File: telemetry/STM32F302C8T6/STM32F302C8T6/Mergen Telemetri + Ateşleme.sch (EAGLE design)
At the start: 91 parts, among them J2 U.FL, Q2 IRLML6344TRPBF, Q3 IRLML6344TRPBF, U2 BMP280, U3 MPU-6050, U4 L86, U6 AMS1117-3.3, U7 AMS1117-3.3, U8 STM32F302C8T6, Y2 ABM3B-26.000MHZ-10-1-U-T

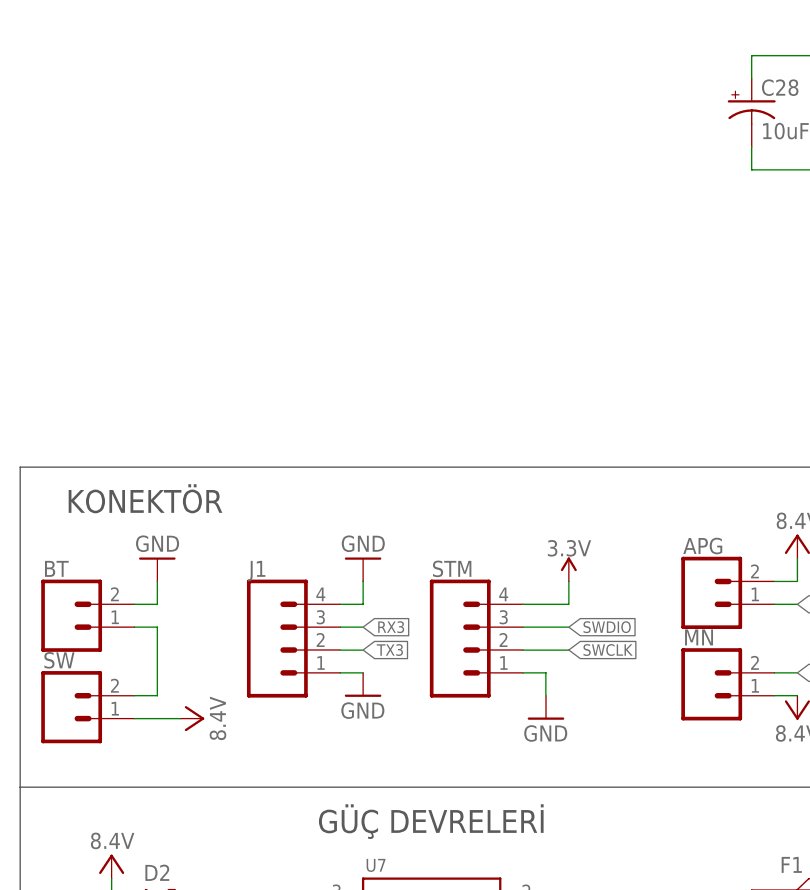
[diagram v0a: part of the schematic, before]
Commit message: Connector was changed and Preparing first order
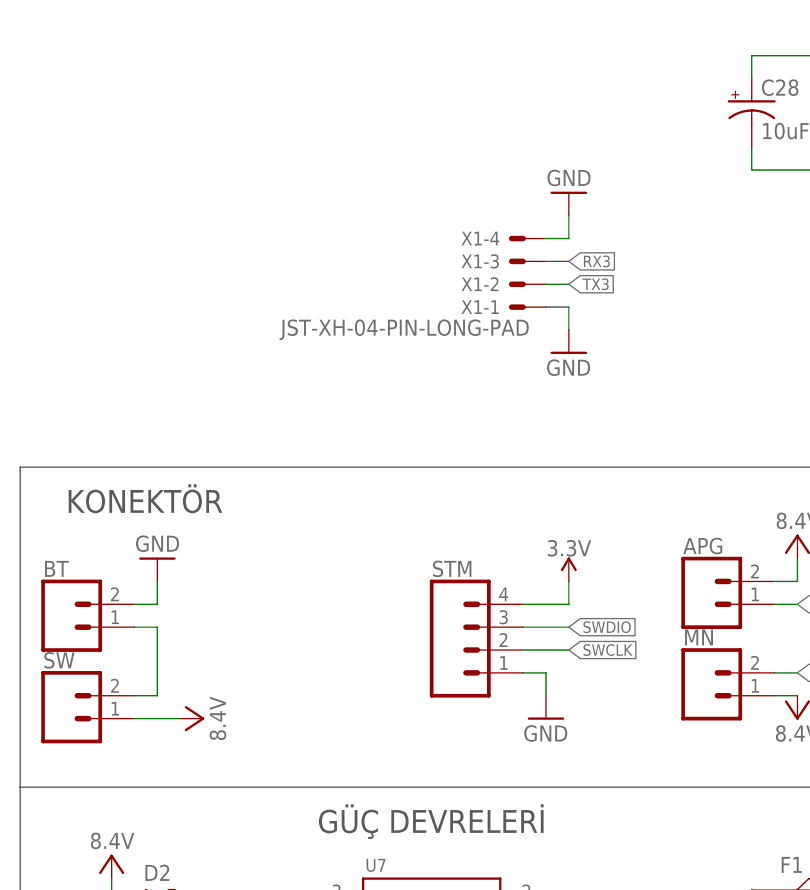
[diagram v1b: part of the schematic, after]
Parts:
- removed J1: (no value), SparkFun-Connectors:CONN_04JST-PTH-VERT
- added X1: JST-XH-04-PIN-LONG-PAD, Rembrandt Electronics - JST XH Connectors v1-0:JST-XH-04-PIN-LONG-PAD
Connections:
- net GND: now also X1-1.S, X1-4.S; no longer J1.1, J1.4
- net RX3: now also X1-3.S; no longer J1.3
- net TX3: now also X1-2.S; no longer J1.2
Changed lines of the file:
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@@
 <part name="ESDA" library="Wurth_EMC Components_WE-TVSP" library_urn="urn:adsk.eagle:library:14283044" deviceset="WE-TVSP_DO-214AC_400W_UNI" device="" package3d_urn="urn:adsk.eagle:package:12146528/2" technology="_824500102" value="12V"/>
 <part name="ESDA1" library="Wurth_EMC Components_WE-TVSP" library_urn="urn:adsk.eagle:library:14283044" deviceset="WE-TVSP_DO-214AC_400W_UNI" device="" package3d_urn="urn:adsk.eagle:package:12146528/2" technology="_824500102" value="12V"/>
-<part name="GND10" library="supply1" library_urn="urn:adsk.eagle:library:371" deviceset="GND" device=""/>
 <part name="SUPPLY17" library="SparkFun-PowerSymbols" library_urn="urn:adsk.eagle:library:530" deviceset="5V" device=""/>
 <part name="C29" library="adafruit" library_urn="urn:adsk.eagle:library:420" deviceset="CPOL-US" device="150CLZ-1010" package3d_urn="urn:adsk.eagle:package:6240454/1" value="1000uF"/>
 <part name="C26" library="adafruit" library_urn="urn:adsk.eagle:library:420" deviceset="CPOL-US" device="150CLZ-1010" package3d_urn="urn:adsk.eagle:package:6240454/1" value="1000uF"/>
 <part name="GND38" library="supply1" library_urn="urn:adsk.eagle:library:371" deviceset="GND" device=""/>
-<part name="J1" library="SparkFun-Connectors" library_urn="urn:adsk.eagle:library:513" deviceset="CONN_04" device="JST-PTH-VERT" package3d_urn="urn:adsk.eagle:package:38102/1"/>
 <part name="D8" library="SparkFun-LED" library_urn="urn:adsk.eagle:library:27167846" deviceset="LED" device="0603" package3d_urn="urn:adsk.eagle:package:27167834/2"/>
 <part name="GND40" library="supply1" library_urn="urn:adsk.eagle:library:371" deviceset="GND" device=""/>
 <part name="GND41" library="supply1" library_urn="urn:adsk.eagle:library:371" deviceset="GND" device=""/>
-<part name="GND2" library="supply1" library_urn="urn:adsk.eagle:library:371" deviceset="GND" device=""/>
 <part name="U2" library="BMP280" deviceset="BMP280" device=""/>
 <part name="SUPPLY6" library="SparkFun-PowerSymbols" library_urn="urn:adsk.eagle:library:530" deviceset="3.3V" device=""/>
@@
 <part name="SUPPLY23" library="SparkFun-PowerSymbols" deviceset="3.3V" device=""/>
 <part name="GND21" library="SparkFun-PowerSymbols" deviceset="GND" device=""/>
+<part name="X1" library="Rembrandt Electronics - JST XH Connectors v1-0" deviceset="JST-XH-04-PIN" device="-LONG-PAD"/>
+<part name="GND8" library="supply1" library_urn="urn:adsk.eagle:library:371" deviceset="GND" device=""/>
+<part name="GND23" library="supply1" library_urn="urn:adsk.eagle:library:371" deviceset="GND" device=""/>
 </parts>
 <sheets>
@@
 <attribute name="VALUE" x="128.27" y="-40.64" size="1.27" layer="96" rot="R90"/>
 </instance>
-<instance part="GND10" gate="1" x="-129.54" y="60.96" smashed="yes">
-<attribute name="VALUE" x="-132.08" y="58.42" size="1.778" layer="96"/>
-</instance>
 <instance part="SUPPLY17" gate="G$1" x="68.58" y="-63.5" smashed="yes">
 <attribute name="VALUE" x="68.58" y="-60.706" size="1.778" layer="96" align="bottom-center"/>
@@
 <attribute name="VALUE" x="66.04" y="-86.36" size="1.778" layer="96"/>
 </instance>
-<instance part="J1" gate="G$1" x="-137.16" y="66.04" smashed="yes">
-<attribute name="VALUE" x="-142.24" y="58.674" size="1.778" layer="96" font="vector"/>
-<attribute name="NAME" x="-142.24" y="74.168" size="1.778" layer="95" font="vector"/>
-</instance>
 <instance part="D8" gate="G$1" x="5.08" y="-76.2" smashed="yes">
 <attribute name="NAME" x="1.651" y="-80.772" size="1.778" layer="95" font="vector" rot="R90"/>
@@
 <attribute name="VALUE" x="35.56" y="-83.82" size="1.778" layer="96"/>
 </instance>
-<instance part="GND2" gate="1" x="-129.54" y="76.2" smashed="yes" rot="R180">
-<attribute name="VALUE" x="-127" y="78.74" size="1.778" layer="96" rot="R180"/>
-</instance>
 <instance part="U2" gate="G$1" x="-50.8" y="-30.48" smashed="yes">
 <attribute name="NAME" x="-60.9796" y="-22.84533125" size="1.78141875" layer="95"/>
@@
 <instance part="GND21" gate="1" x="73.66" y="58.42" smashed="yes">
 <attribute name="VALUE" x="73.66" y="58.166" size="1.778" layer="96" align="top-center"/>
+</instance>
+<instance part="X1" gate="-1" x="-111.76" y="104.14" smashed="yes" rot="R180">
+<attribute name="NAME" x="-114.3" y="104.902" size="1.524" layer="95" rot="R180"/>
+<attribute name="VALUE" x="-110.998" y="102.743" size="1.778" layer="96" rot="R180"/>
+</instance>
+<instance part="X1" gate="-2" x="-111.76" y="106.68" smashed="yes" rot="R180">
+<attribute name="NAME" x="-114.3" y="107.442" size="1.524" layer="95" rot="R180"/>
+</instance>
+<instance part="X1" gate="-3" x="-111.76" y="109.22" smashed="yes" rot="R180">
+<attribute name="NAME" x="-114.3" y="109.982" size="1.524" layer="95" rot="R180"/>
+</instance>
+<instance part="X1" gate="-4" x="-111.76" y="111.76" smashed="yes" rot="R180">
+<attribute name="NAME" x="-114.3" y="112.522" size="1.524" layer="95" rot="R180"/>
+</instance>
+<instance part="GND8" gate="1" x="-106.68" y="116.84" smashed="yes" rot="R180">
+<attribute name="VALUE" x="-104.14" y="119.38" size="1.778" layer="96" rot="R180"/>
+</instance>
+<instance part="GND23" gate="1" x="-106.68" y="99.06" smashed="yes">
+<attribute name="VALUE" x="-109.22" y="96.52" size="1.778" layer="96"/>
 </instance>
 </instances>
@@
 </segment>
 <segment>
-<pinref part="GND10" gate="1" pin="GND"/>
-<pinref part="J1" gate="G$1" pin="1"/>
-<wire x1="-132.08" y1="63.5" x2="-129.54" y2="63.5" width="0.1524" layer="91"/>
-</segment>
-<segment>
 <pinref part="C29" gate="G$1" pin="-"/>
 <pinref part="GND38" gate="1" pin="GND"/>
@@
 </segment>
 <segment>
-<pinref part="J1" gate="G$1" pin="4"/>
-<wire x1="-132.08" y1="71.12" x2="-129.54" y2="71.12" width="0.1524" layer="91"/>
-<pinref part="GND2" gate="1" pin="GND"/>
-<wire x1="-129.54" y1="71.12" x2="-129.54" y2="73.66" width="0.1524" layer="91"/>
-</segment>
-<segment>
 <pinref part="U2" gate="G$1" pin="GND"/>
 <wire x1="-38.1" y1="-35.56" x2="-35.56" y2="-35.56" width="0.1524" layer="91"/>
@@
 <wire x1="71.12" y1="63.5" x2="73.66" y2="63.5" width="0.1524" layer="91"/>
 <junction x="73.66" y="63.5"/>
+</segment>
+<segment>
+<pinref part="X1" gate="-4" pin="S"/>
+<wire x1="-109.22" y1="111.76" x2="-106.68" y2="111.76" width="0.1524" layer="91"/>
+<pinref part="GND8" gate="1" pin="GND"/>
+<wire x1="-106.68" y1="111.76" x2="-106.68" y2="114.3" width="0.1524" layer="91"/>
+</segment>
+<segment>
+<pinref part="X1" gate="-1" pin="S"/>
+<wire x1="-109.22" y1="104.14" x2="-106.68" y2="104.14" width="0.1524" layer="91"/>
+<pinref part="GND23" gate="1" pin="GND"/>
+<wire x1="-106.68" y1="104.14" x2="-106.68" y2="101.6" width="0.1524" layer="91"/>
 </segment>
 </net>
@@
 </segment>
 <segment>
-<label x="-129.54" y="66.04" size="1.27" layer="95" xref="yes"/>
-<pinref part="J1" gate="G$1" pin="2"/>
-<wire x1="-132.08" y1="66.04" x2="-129.54" y2="66.04" width="0.1524" layer="91"/>
+<pinref part="X1" gate="-2" pin="S"/>
+<wire x1="-109.22" y1="106.68" x2="-106.68" y2="106.68" width="0.1524" layer="91"/>
+<label x="-106.68" y="106.68" size="1.27" layer="95" xref="yes"/>
 </segment>
 </net>
@@
 </segment>
 <segment>
-<label x="-129.54" y="68.58" size="1.27" layer="95" xref="yes"/>
-<pinref part="J1" gate="G$1" pin="3"/>
-<wire x1="-132.08" y1="68.58" x2="-129.54" y2="68.58" width="0.1524" layer="91"/>
-</segment>
-</net>
+<pinref part="X1" gate="-3" pin="S"/>
+<wire x1="-109.22" y1="109.22" x2="-106.68" y2="109.22" width="0.1524" layer="91"/>
+<label x="-106.68" y="109.22" size="1.27" layer="95" xref="yes"/>
+</segment>
+</net>

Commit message: Polygon witdh was increased IMPORTANT
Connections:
- net 3.3V: now also X1-4.S
- net GND: no longer X1-4.S
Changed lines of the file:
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@@
 <part name="GND21" library="SparkFun-PowerSymbols" deviceset="GND" device=""/>
 <part name="X1" library="Rembrandt Electronics - JST XH Connectors v1-0" deviceset="JST-XH-04-PIN" device="-LONG-PAD"/>
-<part name="GND8" library="supply1" library_urn="urn:adsk.eagle:library:371" deviceset="GND" device=""/>
 <part name="GND23" library="supply1" library_urn="urn:adsk.eagle:library:371" deviceset="GND" device=""/>
+<part name="SUPPLY13" library="SparkFun-PowerSymbols" library_urn="urn:adsk.eagle:library:530" deviceset="3.3V" device=""/>
 </parts>
 <sheets>
@@
 <attribute name="NAME" x="-114.3" y="112.522" size="1.524" layer="95" rot="R180"/>
 </instance>
-<instance part="GND8" gate="1" x="-106.68" y="116.84" smashed="yes" rot="R180">
-<attribute name="VALUE" x="-104.14" y="119.38" size="1.778" layer="96" rot="R180"/>
-</instance>
 <instance part="GND23" gate="1" x="-106.68" y="99.06" smashed="yes">
 <attribute name="VALUE" x="-109.22" y="96.52" size="1.778" layer="96"/>
+</instance>
+<instance part="SUPPLY13" gate="G$1" x="-106.68" y="114.3" smashed="yes">
+<attribute name="VALUE" x="-106.68" y="117.094" size="1.778" layer="96" align="bottom-center"/>
 </instance>
 </instances>
@@
 </segment>
 <segment>
-<pinref part="X1" gate="-4" pin="S"/>
-<wire x1="-109.22" y1="111.76" x2="-106.68" y2="111.76" width="0.1524" layer="91"/>
-<pinref part="GND8" gate="1" pin="GND"/>
-<wire x1="-106.68" y1="111.76" x2="-106.68" y2="114.3" width="0.1524" layer="91"/>
-</segment>
-<segment>
 <pinref part="X1" gate="-1" pin="S"/>
 <wire x1="-109.22" y1="104.14" x2="-106.68" y2="104.14" width="0.1524" layer="91"/>
@@
 <wire x1="2.54" y1="58.42" x2="10.16" y2="58.42" width="0.1524" layer="91"/>
 </segment>
-</net>
+<segment>
+<pinref part="X1" gate="-4" pin="S"/>
+<wire x1="-109.22" y1="111.76" x2="-106.68" y2="111.76" width="0.1524" layer="91"/>
+<pinref part="SUPPLY13" gate="G$1" pin="3.3V"/>
+<wire x1="-106.68" y1="111.76" x2="-106.68" y2="114.3" width="0.1524" layer="91"/>
+</segment>
+</net>
